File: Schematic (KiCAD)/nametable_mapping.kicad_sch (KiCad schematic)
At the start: 40 parts

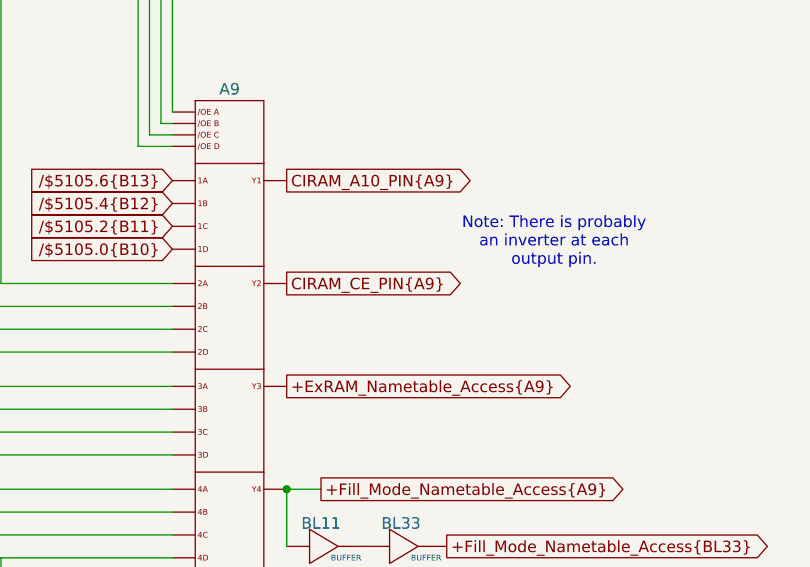
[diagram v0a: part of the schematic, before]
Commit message: - All known gates and traces are now accounted for in the schematics!  :)
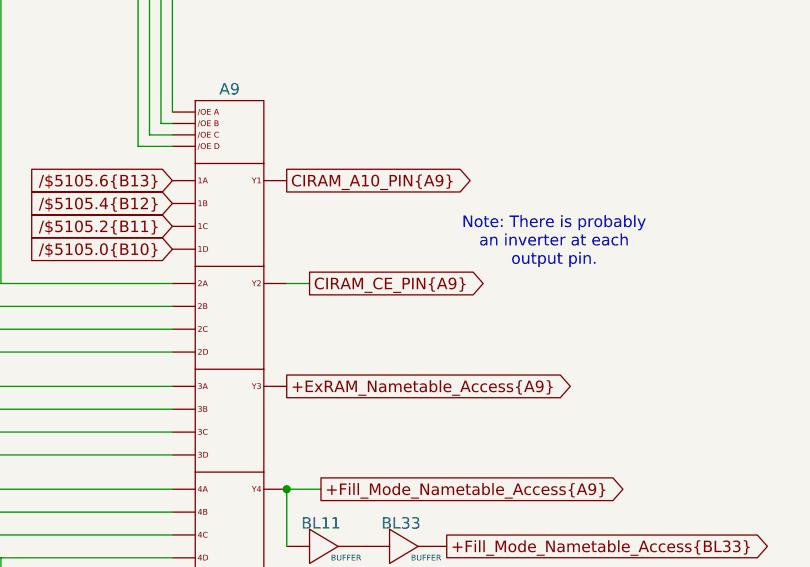
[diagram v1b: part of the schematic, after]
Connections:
- new net: B9. (X), C1. (/Q7)
- new net: A13. (X), A14. (X), B18. (X), B19. (X), B20. (X), B21. (X), B22. (X), B23. (X), B24. (X), B25. (X)
- new net: A9. (Y4), B25. (X)
- new net: B6. (X), C1. (/Q7)
- new net: A9. (Y4), B23. (X)
- new net: A16. (X), B14. (X), B15. (X), B16. (X), B17. (X)
- new net: A13. (X), B14. (X), B15. (X), B16. (X), B17. (X)
- new net: A9. (Y4), B16. (X)
- new net: B10. (X), C1. (/Q7)
- new net: A9. (Y4), B15. (X)
- new net: B7. (X), C1. (/Q7)
- new net: A11. (X), A12. (X)
- new net: A10. (X), A11. (X)
- new net: B4. (X), C1. (/Q7)
- new net: BL11. (X), BL33. (X)
- new net: B11. (X), C1. (/Q7)
- new net: B3. (X), C1. (/Q7)
- new net: A9. (Y4), B22. (X)
- new net: A17. (X), C1. (/Q7)
- new net: A9. (Y4), B14. (X)
- new net: A9. (Y4), B21. (X)
- new net: A9. (Y4), B18. (X)
- new net: A9. (Y4), B20. (X)
- new net: A9. (Y4), B19. (X)
- new net: A9. (Y4), B17. (X)
- new net: A9. (Y4), B24. (X)
- new net: B13. (X), C1. (/Q7)
- new net: B12. (X), C1. (/Q7)
- new net: B5. (X), C1. (/Q7)
- new net: B8. (X), C1. (/Q7)
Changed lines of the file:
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@@
+	(wire
+		(pts
+			(xy 238.76 102.87) (xy 236.22 102.87)
+		)
+		(stroke
+			(width 0)
+			(type default)
+		)
+	)
 	(wire
 		(pts
@@
 	(global_label "CIRAM_CE_PIN{A9}"
 		(shape output)
-		(at 236.22 102.87 0)
-		(fields_autoplaced yes)
-		(effects
-			(font
-				(size 1.27 1.27)
-			)
-			(justify left)
-		)
-		(property "Intersheetrefs" "${INTERSHEET_REFS}"
-			(at 256.441 102.87 0)
-			(effects
-				(font
+		(at 238.76 102.87 0)
+		(fields_autoplaced yes)
+		(effects
+			(font
+				(size 1.27 1.27)
+			)
+			(justify left)
+		)
+		(property "Intersheetrefs" "${INTERSHEET_REFS}"
+			(at 258.981 102.87 0)
+			(effects
+				(font
